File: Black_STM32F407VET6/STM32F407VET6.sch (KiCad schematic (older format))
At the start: 96 parts, among them J1 T0, J10 - HotBed +, J11 Heater0, J12 X-, J13 Y-, J14 Z-, J15 Z+, J16 USB_B, J17 LeftSpi, J18 EXTRAPINS, J2 T1, J23 EXP2, J24 LCD2004, J25 Bottom, J26 Right, J28 LIGHTS, J29 Z, J3 TB, J30 Z, J38 X, J39 Y, J4 TC, J41 E0, J43 Heater1, J44 COM, J47 I2C, J48 SPI, J49 SPI, J5 + VIN -, J50 SDIO, J51 Servo, J52 Servo, J53 PowerSelect, J54 Power, J55 PD11, J56 Power, J6 Fan3, J7 Fan2, J8 Fan1, J9 Fan0, Q1 BCX70, Q10 BCX70, Q11 BCX70, Q12 IRLR8726PBF, Q13 IRLR8726PBF, Q14 IRLR8726PBF, Q2 BCX70, Q3 BCX70, Q4 IRLML0030TRPBF, Q5 BCX70, Q6 IRLML0030TRPBF, Q7 IRLML0030TRPBF, Q8 IRLML0030TRPBF, Q9 BCX70, SW1 Boot0, U1 LeftAnalog, U2 Left5V, U5 AT24CS01-SSHM

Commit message: Wider tracks, more clearance, X & Y logic. 	SPI 1 is no longer used on shield because is used on the mcu board with different pins 	Added a design rule, distance between tracks is now at least 0.2925 	Wired X and Y driver logic with pin changes. 	Added a buck convertor spot with external connections in the meantime 	Stepper drivers are now consistently spaced from each other.
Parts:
- added J19: 12Vinput, Connector_PinHeader_2.54mm:PinHeader_1x03_P2.54mm_Vertical, symbol Connector_Generic:Conn_01x03
- added J20: 5VOut, Connector_PinHeader_2.54mm:PinHeader_1x01_P2.54mm_Vertical, symbol Connector_Generic:Conn_01x01
- added U3: BuckConvertor, Motor_driver:MP2307Buck, symbol STM32F407VET6:BuckConvertor
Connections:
- net labels added: PD6
- net labels removed: PA4
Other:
- moved on the sheet: J10, J56
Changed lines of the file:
@@
 L Connector_Generic:Conn_01x03 J56
 U 1 1 5C700CF8
-P 14850 7950
-F 0 "J56" H 15000 8000 50  0000 C CNN
-F 1 "Power" H 15050 7900 50  0000 C CNN
-F 2 "Connector_PinHeader_2.54mm:PinHeader_1x03_P2.54mm_Vertical" H 14850 7950 50  0001 C CNN
-F 3 "~" H 14850 7950 50  0001 C CNN
-	1    14850 7950
+P 14000 8750
+F 0 "J56" H 14150 8800 50  0000 C CNN
+F 1 "Power" H 14200 8700 50  0000 C CNN
+F 2 "Connector_PinHeader_2.54mm:PinHeader_1x03_P2.54mm_Vertical" H 14000 8750 50  0001 C CNN
+F 3 "~" H 14000 8750 50  0001 C CNN
+	1    14000 8750
 	-1   0    0    -1
 $EndComp
@@
 L power:+5V #PWR0105
 U 1 1 5D491BB6
-P 15500 7750
-F 0 "#PWR0105" H 15500 7600 50  0001 C CNN
-F 1 "+5V" H 15515 7923 50  0000 C CNN
-F 2 "" H 15500 7750 50  0001 C CNN
-F 3 "" H 15500 7750 50  0001 C CNN
-	1    15500 7750
+P 14650 8550
+F 0 "#PWR0105" H 14650 8400 50  0001 C CNN
+F 1 "+5V" H 14665 8723 50  0000 C CNN
+F 2 "" H 14650 8550 50  0001 C CNN
+F 3 "" H 14650 8550 50  0001 C CNN
+	1    14650 8550
 	1    0    0    -1
 $EndComp
@@
 L power:+12V #PWR0106
 U 1 1 5D487131
-P 15200 7750
-F 0 "#PWR0106" H 15215 8015 50  0001 C CNN
-F 1 "+12V" H 15215 7923 50  0000 C CNN
-F 2 "" H 15200 7750 50  0001 C CNN
-F 3 "" H 15200 7750 50  0001 C CNN
-	1    15200 7750
+P 14350 8550
+F 0 "#PWR0106" H 14365 8815 50  0001 C CNN
+F 1 "+12V" H 14365 8723 50  0000 C CNN
+F 2 "" H 14350 8550 50  0001 C CNN
+F 3 "" H 14350 8550 50  0001 C CNN
+	1    14350 8550
 	1    0    0    -1
 $EndComp
@@
 Connection ~ 1800 5450
 Wire Wire Line
-	15050 7850 15200 7850
-Wire Wire Line
-	15200 7850 15200 7750
+	14200 8650 14350 8650
+Wire Wire Line
+	14350 8650 14350 8550
 $Comp
 L power:GND #PWR0109
 U 1 1 5D265062
-P 15200 8150
-F 0 "#PWR0109" H 15200 7900 50  0001 C CNN
-F 1 "GND" H 15205 7977 50  0000 C CNN
-F 2 "" H 15200 8150 50  0001 C CNN
-F 3 "" H 15200 8150 50  0001 C CNN
-	1    15200 8150
+P 14350 8950
+F 0 "#PWR0109" H 14350 8700 50  0001 C CNN
+F 1 "GND" H 14355 8777 50  0000 C CNN
+F 2 "" H 14350 8950 50  0001 C CNN
+F 3 "" H 14350 8950 50  0001 C CNN
+	1    14350 8950
 	1    0    0    -1
 $EndComp
@@
 $EndComp
 Wire Wire Line
-	15050 7950 15200 7950
-Wire Wire Line
-	15200 7950 15200 8150
-Wire Wire Line
-	15050 8050 15500 8050
-Wire Wire Line
-	15500 8050 15500 7750
+	14200 8750 14350 8750
+Wire Wire Line
+	14350 8750 14350 8950
+Wire Wire Line
+	14200 8850 14650 8850
+Wire Wire Line
+	14650 8850 14650 8550
 $Comp
 L Connector:Screw_Terminal_01x02 J5
@@
 L Connector_Generic:Conn_01x02 J10
 U 1 1 5D53C77B
-P 5800 1400
-F 0 "J10" H 5880 1392 50  0000 L CNN
-F 1 "- HotBed +" H 5880 1301 50  0000 L CNN
-F 2 "SH_Connectors:KF7.62_2P" H 5800 1400 50  0001 C CNN
-F 3 "~" H 5800 1400 50  0001 C CNN
-	1    5800 1400
+P 5400 1400
+F 0 "J10" H 5480 1392 50  0000 L CNN
+F 1 "- HotBed +" H 5480 1301 50  0000 L CNN
+F 2 "SH_Connectors:KF7.62_2P" H 5400 1400 50  0001 C CNN
+F 3 "~" H 5400 1400 50  0001 C CNN
+	1    5400 1400
 	1    0    0    -1
 $EndComp
@@
 Text GLabel 13000 3150 2    50   Input ~ 0
 SDIO_CMD
-Text GLabel 13000 2950 2    50   Input ~ 0
-Y_En
 Text GLabel 11600 5600 3    50   Input ~ 0
 X-
@@
 Text GLabel 10500 3100 2    50   Input ~ 0
 TC
-Text GLabel 10500 3000 2    50   Input ~ 0
+Text GLabel 10500 2900 2    50   Input ~ 0
 Y_Dir
-Text GLabel 10500 2900 2    50   Input ~ 0
+Text GLabel 9800 2900 0    50   Input ~ 0
 Y_Step
 Text GLabel 10500 3400 2    50   Input ~ 0
@@
 Text GLabel 9800 3500 0    50   Input ~ 0
 Heater0
-Text GLabel 9800 2800 0    50   Input ~ 0
+Text GLabel 9800 3400 0    50   Input ~ 0
 X_Step
 Text GLabel 9800 3000 0    50   Input ~ 0
 X_En
-Text GLabel 9800 2900 0    50   Input ~ 0
+Text GLabel 10500 3000 2    50   Input ~ 0
 X_CS
 Text GLabel 10500 3700 2    50   Input ~ 0
@@
 Wire Wire Line
 	10500 3600 11300 3600
-Text GLabel 9800 3600 0    50   Input ~ 0
-PA4
-Text GLabel 11300 3400 0    50   Input ~ 0
-PA4
 Text GLabel 9800 3700 0    50   Input ~ 0
 PA6
 Text GLabel 11300 3500 0    50   Input ~ 0
 PA6
-Text GLabel 9800 3400 0    50   Input ~ 0
+Text GLabel 9800 3600 0    50   Input ~ 0
 X_Dir
 Text GLabel 11300 3700 0    50   Input ~ 0
@@
 Text GLabel 9800 3800 0    50   Input ~ 0
 PC4
+$Comp
+L STM32F407VET6:BuckConvertor U3
+U 1 1 5D338CA3
+P 8950 9250
+F 0 "U3" H 8950 9575 50  0000 C CNN
+F 1 "BuckConvertor" H 8950 9484 50  0000 C CNN
+F 2 "Motor_driver:MP2307Buck" H 8950 9550 50  0001 C CNN
+F 3 "" H 8950 9550 50  0001 C CNN
+	1    8950 9250
+	1    0    0    -1
+$EndComp
+Text GLabel 8500 9150 0    50   Input ~ 0
+12V
+Text GLabel 8500 9350 0    50   Input ~ 0
+GND
+Text GLabel 9400 9150 2    50   Input ~ 0
+5V
+Text GLabel 9400 9350 2    50   Input ~ 0
+GND
+$Comp
+L Connector_Generic:Conn_01x03 J19
+U 1 1 5D39F163
+P 8650 9750
+F 0 "J19" H 8730 9792 50  0000 L CNN
+F 1 "12Vinput" H 8730 9701 50  0000 L CNN
+F 2 "Connector_PinHeader_2.54mm:PinHeader_1x03_P2.54mm_Vertical" H 8650 9750 50  0001 C CNN
+F 3 "~" H 8650 9750 50  0001 C CNN
+	1    8650 9750
+	1    0    0    -1
+$EndComp
+$Comp
+L Connector_Generic:Conn_01x01 J20
+U 1 1 5D3A136D
+P 9450 9800
+F 0 "J20" H 9368 9575 50  0000 C CNN
+F 1 "5VOut" H 9368 9666 50  0000 C CNN
+F 2 "Connector_PinHeader_2.54mm:PinHeader_1x01_P2.54mm_Vertical" H 9368 9667 50  0001 C CNN
+F 3 "~" H 9450 9800 50  0001 C CNN
+	1    9450 9800
+	-1   0    0    1
+$EndComp
+Text GLabel 8450 9750 0    50   Input ~ 0
+12V
+Text GLabel 8450 9650 0    50   Input ~ 0
+GND
+Text GLabel 8450 9850 0    50   Input ~ 0
+GND
+Text GLabel 9650 9800 2    50   Input ~ 0
+5V
+Text GLabel 9800 2800 0    50   Input ~ 0
+Y_En
+Text GLabel 13000 2950 2    50   Input ~ 0
+PD6
+Text GLabel 11300 3400 0    50   Input ~ 0
+PD6
 $EndSCHEMATC

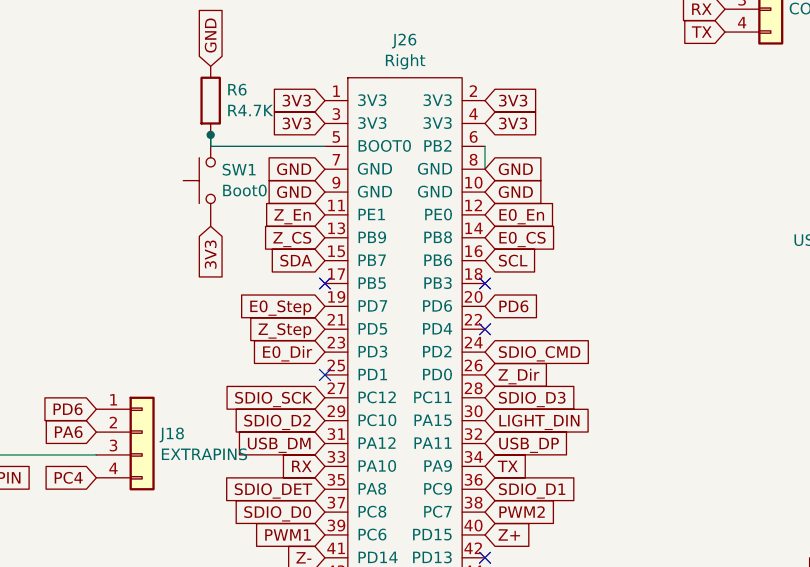
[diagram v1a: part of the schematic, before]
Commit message: Z and E0 wiring 	- 12V rails 	- TODO: spi lines
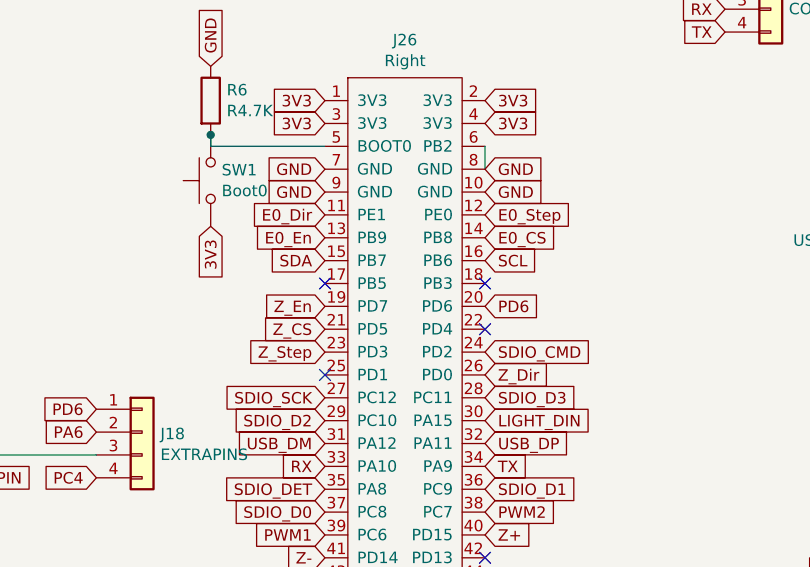
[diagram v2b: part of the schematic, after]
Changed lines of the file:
@@
 Text GLabel 12300 3750 0    50   Input ~ 0
 SDIO_DET
-Text GLabel 12300 2950 0    50   Input ~ 0
-E0_Step
-Text GLabel 12300 3150 0    50   Input ~ 0
-E0_Dir
 Text GLabel 13000 3250 2    50   Input ~ 0
 Z_Dir
-Text GLabel 12300 3050 0    50   Input ~ 0
+Text GLabel 12300 3150 0    50   Input ~ 0
 Z_Step
-Text GLabel 13000 2550 2    50   Input ~ 0
+Text GLabel 12300 2650 0    50   Input ~ 0
 E0_En
-Text GLabel 12300 2550 0    50   Input ~ 0
+Text GLabel 12300 2950 0    50   Input ~ 0
 Z_En
 NoConn ~ 13000 3050
@@
 Text GLabel 13000 3650 2    50   Input ~ 0
 TX
-Text GLabel 13000 2750 2    50   Input ~ 0
-SCL
-Text GLabel 12300 2750 0    50   Input ~ 0
-SDA
 Text GLabel 12300 3550 0    50   Input ~ 0
 USB_DM
@@
 Text GLabel 15600 2650 2    50   Input ~ 0
 USB_DP
-Text GLabel 12300 2650 0    50   Input ~ 0
+Text GLabel 12300 3050 0    50   Input ~ 0
 Z_CS
 Text GLabel 13000 2650 2    50   Input ~ 0
@@
 F 3 "~" H 15050 4100 50  0001 C CNN
 	1    15050 4100
-	1    0    0    -1
-$EndComp
-$Comp
-L STM32F407VET6:Right J26
-U 1 1 5D30CC8F
-P 12650 3200
-F 0 "J26" H 12650 4615 50  0000 C CNN
-F 1 "Right" H 12650 4524 50  0000 C CNN
-F 2 "Connector_PinSocket_2.54mm:PinSocket_2x24_P2.54mm_Vertical" H 12650 2850 50  0001 C CNN
-F 3 "" H 12650 2850 50  0001 C CNN
-	1    12650 3200
 	1    0    0    -1
 $EndComp
@@
 Text GLabel 11300 3400 0    50   Input ~ 0
 PD6
+$Comp
+L STM32F407VET6:Right J26
+U 1 1 5D30CC8F
+P 12650 3200
+F 0 "J26" H 12650 4615 50  0000 C CNN
+F 1 "Right" H 12650 4524 50  0000 C CNN
+F 2 "Connector_PinSocket_2.54mm:PinSocket_2x24_P2.54mm_Vertical" H 12650 2850 50  0001 C CNN
+F 3 "" H 12650 2850 50  0001 C CNN
+	1    12650 3200
+	1    0    0    -1
+$EndComp
+Text GLabel 12300 2750 0    50   Input ~ 0
+SDA
+Text GLabel 12300 2550 0    50   Input ~ 0
+E0_Dir
+Text GLabel 13000 2550 2    50   Input ~ 0
+E0_Step
+Text GLabel 13000 2750 2    50   Input ~ 0
+SCL
 $EndSCHEMATC

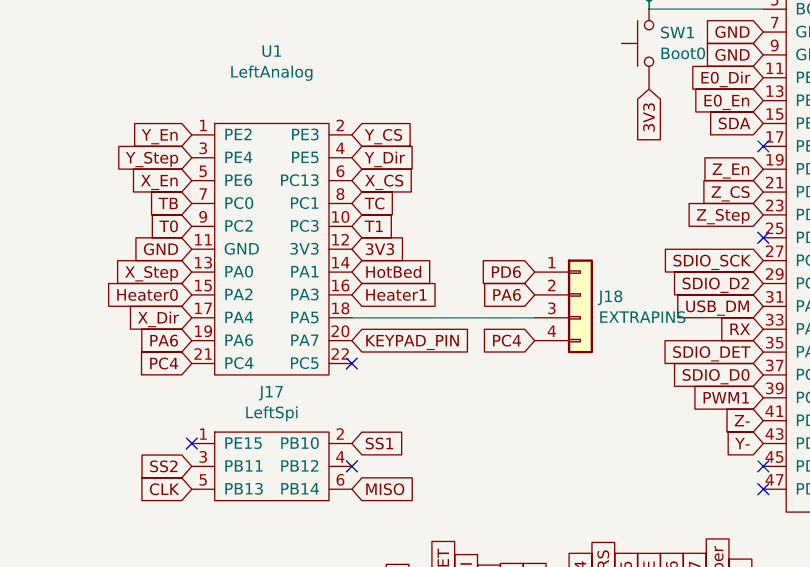
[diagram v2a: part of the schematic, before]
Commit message: Power mosfets  - everything done apart from connecting GND  - Are the 12V rail caps necessary ?
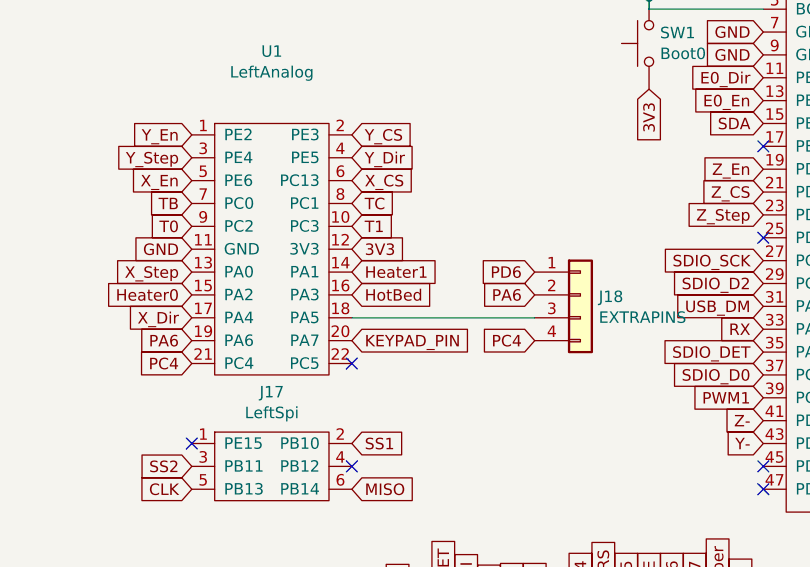
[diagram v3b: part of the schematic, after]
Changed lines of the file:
@@
 Text GLabel 9800 2900 0    50   Input ~ 0
 Y_Step
+Text GLabel 10500 3500 2    50   Input ~ 0
+HotBed
 Text GLabel 10500 3400 2    50   Input ~ 0
-HotBed
-Text GLabel 10500 3500 2    50   Input ~ 0
 Heater1
 Text GLabel 10500 2800 2    50   Input ~ 0
